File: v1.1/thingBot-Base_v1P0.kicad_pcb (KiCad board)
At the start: 2 copper layers, 45.5 x 53 mm, 78 parts, among them P1 Micro_usb_B, P2 BATT_CONN, P3 XBEE_CONN_LEFT, P4 CONN_01X02, P5 CONN_01X02, P6 JTAG, P7 XBEE, P8 XBEE_CONN_RIGHT, SW1 ON/OFF_Switch, U2 CP2102, U3 LP5907_LDO_250mA, U4 PROBE

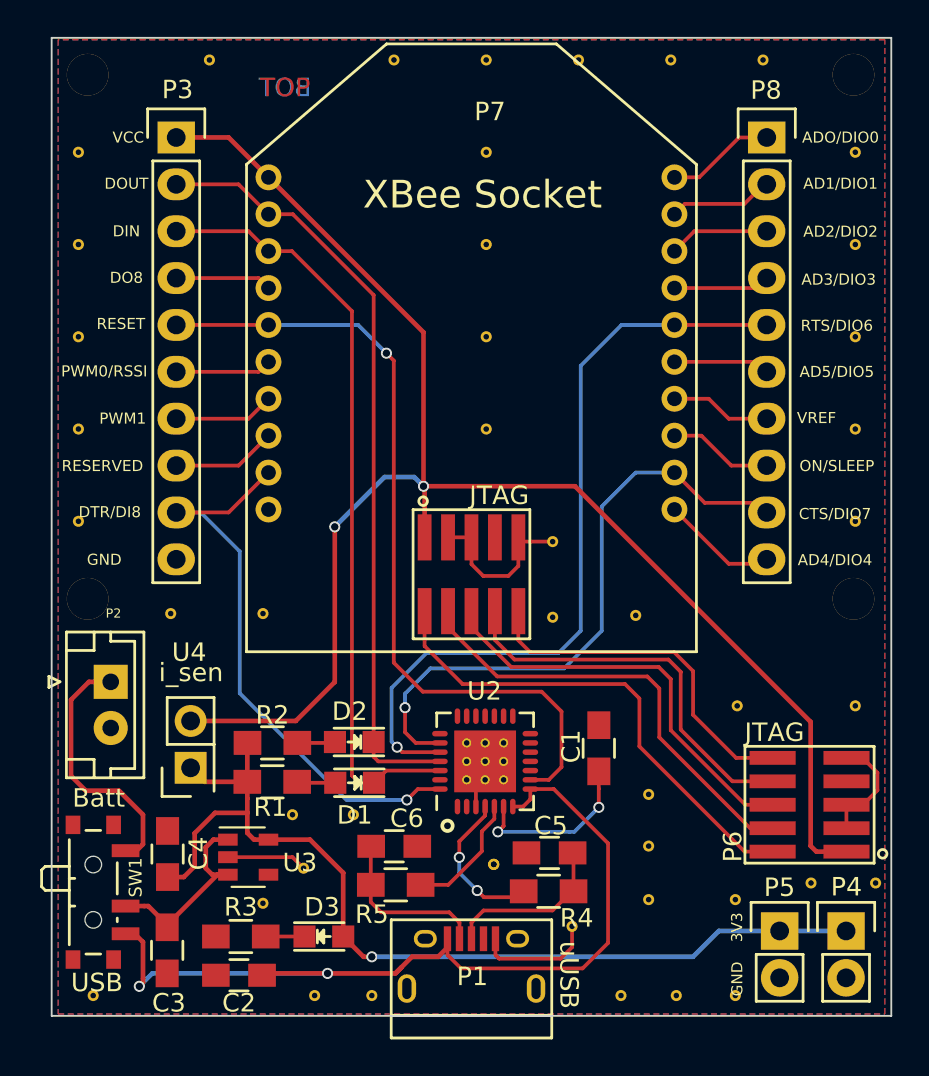
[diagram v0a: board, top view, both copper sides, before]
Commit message: thingBot-Base v1.1 all files added
in v1.1 these thing Added
- JST connector pins changed
- 1x2 2.54mm headers alighned properly
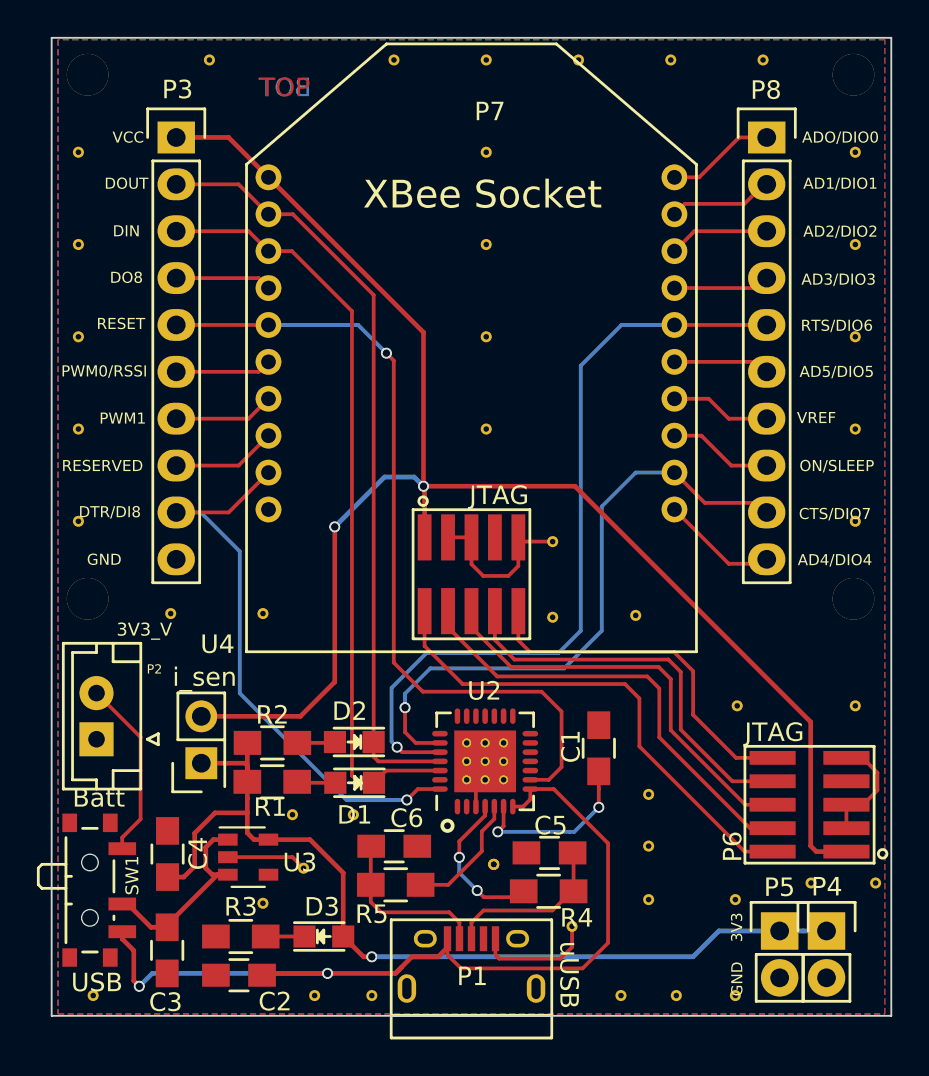
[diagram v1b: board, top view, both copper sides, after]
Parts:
- moved P2 3.20 mm to (128.7, 107.6), turned to 90 degrees
- moved P4 1.06 mm to (168.2, 118.0)
- moved U4 0.63 mm to (134.4, 108.9)
- moved SW1 0.21 mm to (128.7, 115.8)
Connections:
- P2 pad 1: Net-(P2-Pad1) -> GND
- P2 pad 2: GND -> Net-(P2-Pad2)
- SW1 pad 1: Net-(P2-Pad1) -> Net-(P2-Pad2)
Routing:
- net Net-(P2-Pad1): track 14.1 -> 0.00 mm
- net Net-(P2-Pad2): track 0.00 -> 9.83 mm
- net +3V3: track 53.3 -> 52.3 mm
- net VXBEE_3V3: track 87.2 -> 86.5 mm
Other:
- board text added: "3V3_V"
- board text added: "v1.1"
- board text removed: "v1.0"
